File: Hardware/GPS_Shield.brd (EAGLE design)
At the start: 59.7 x 53.3 mm, 52 parts, among them J1 ARDUINO_R3_SHIELD, J2 USD_CONNECTOR, J3 DNP (GP-735-VERTICAL), U1 APK2112-3.3V, U2 GP3906-TLP, U3 TXB0108

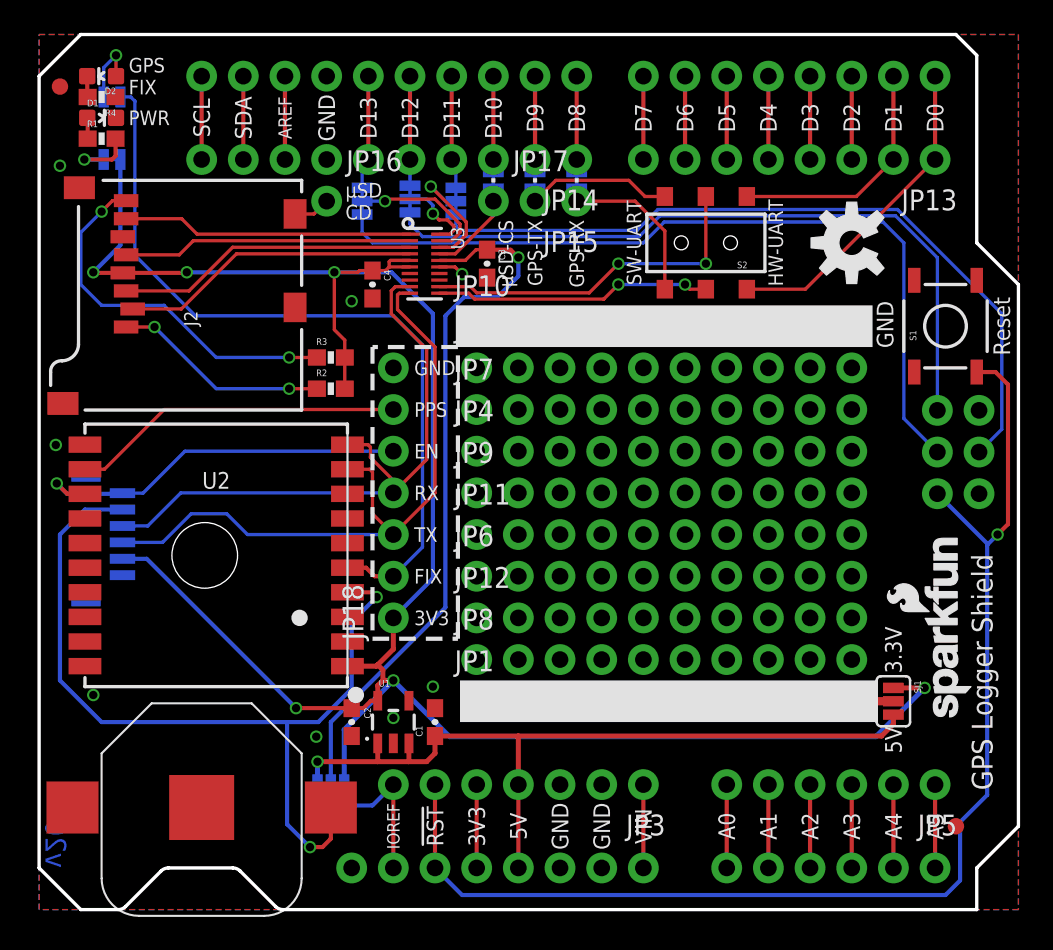
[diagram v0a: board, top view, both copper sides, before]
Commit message: Adding VBATT-to-3.3V jumper, breaking out VBATT.
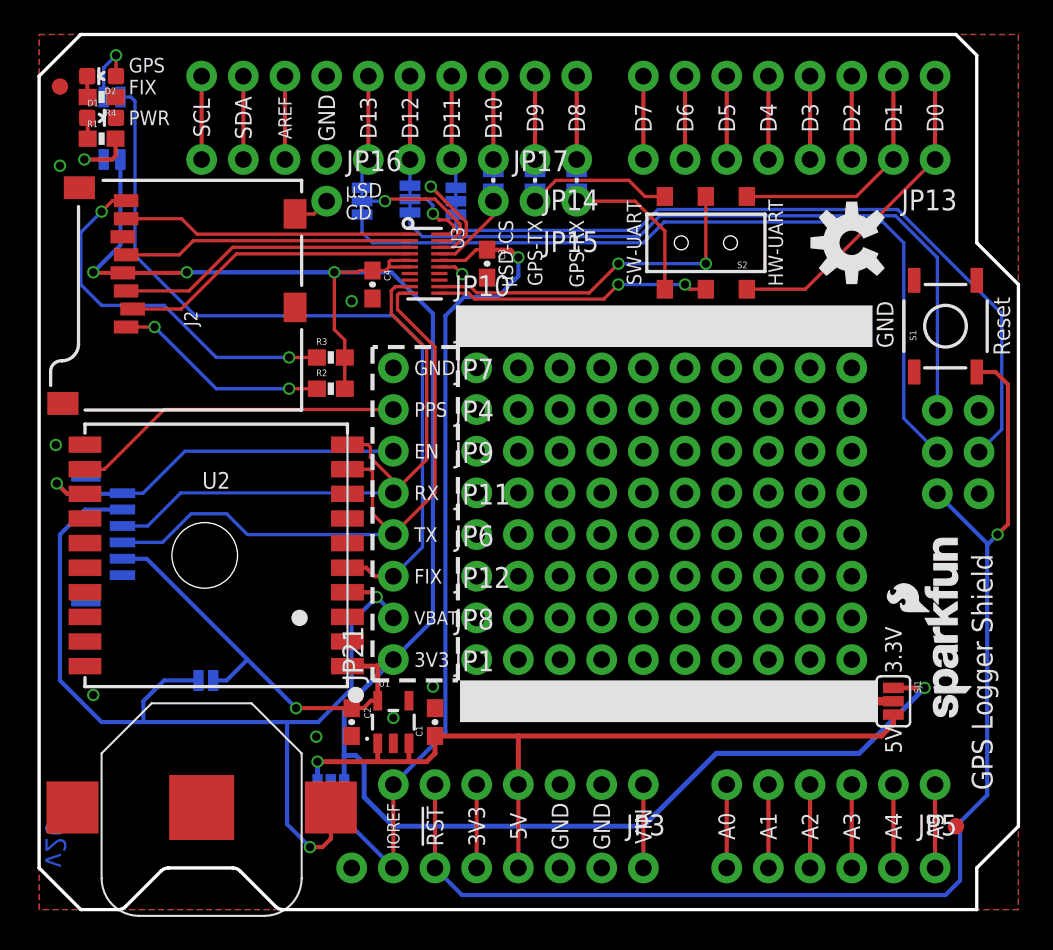
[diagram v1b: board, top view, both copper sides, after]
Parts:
- removed JP18: (no value), SparkFun-Connectors:1X07_NO_SILK
- added JP21: (no value), SparkFun-Connectors:1X08_NO_SILK
- added SJ11: Batt-3v3, SparkFun-Passives:PAD-JUMPER-2-NO_YES_SILK
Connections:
- net 3.3V: now also JP21.1, SJ11.1; no longer JP18.1
- net GND: now also JP21.8; no longer JP18.7
- net GPS_FIX: now also JP21.3; no longer JP18.2
- net GPS_RST: now also JP21.6; no longer JP18.5
- net GPS_RX: now also JP21.5; no longer JP18.4
- net GPS_TX: now also JP21.4; no longer JP18.3
- net PPS: now also JP21.7; no longer JP18.6
- net V_BATT: now also JP21.2, SJ11.2
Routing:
- net 3.3V: track 135.1 -> 145.2 mm, vias 6 -> 5
- net V_BATT: track 52.7 -> 59.6 mm
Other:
- board text added: "Batt"
- board text added: "No Battery"
- board text added: "VBAT"

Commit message: Changing DRU to SparkFun-2-Layer-Tight, slightly moving traces to accomodate.
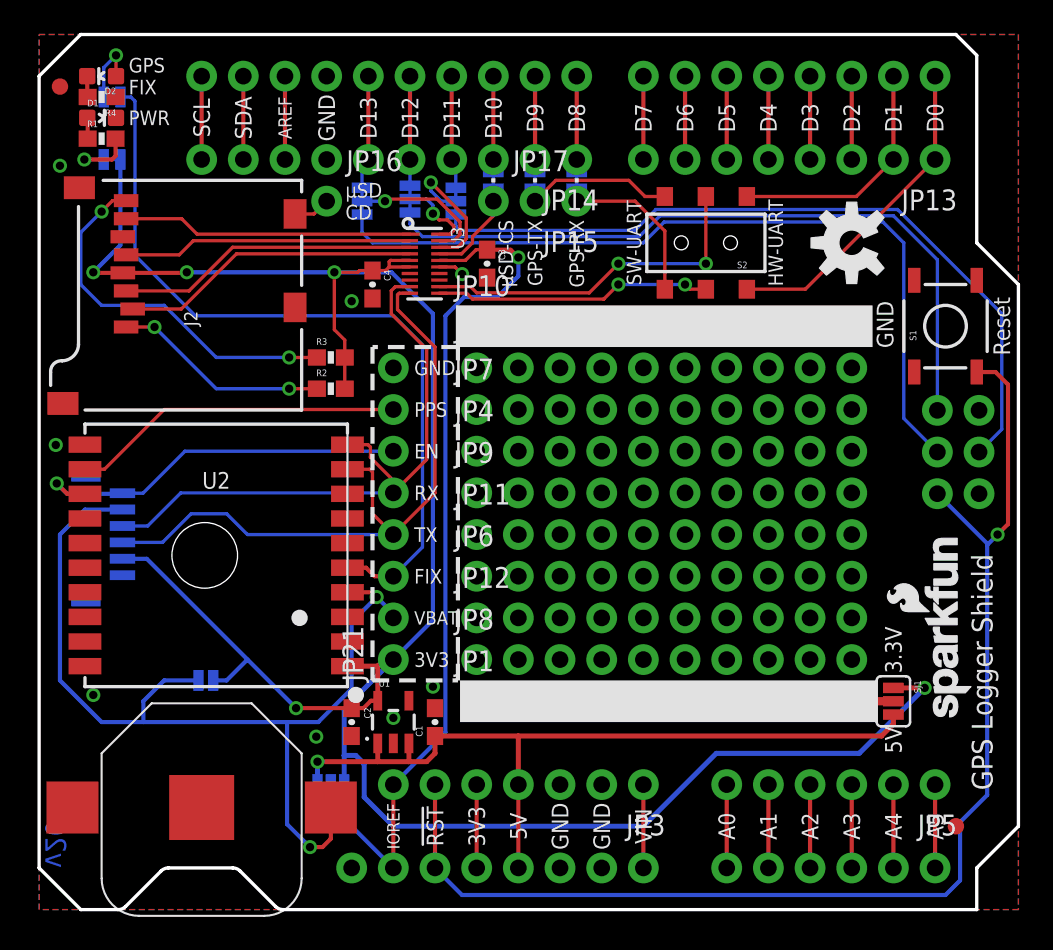
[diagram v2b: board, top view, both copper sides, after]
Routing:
- net HV_MOSI: track 7.67 -> 8.48 mm

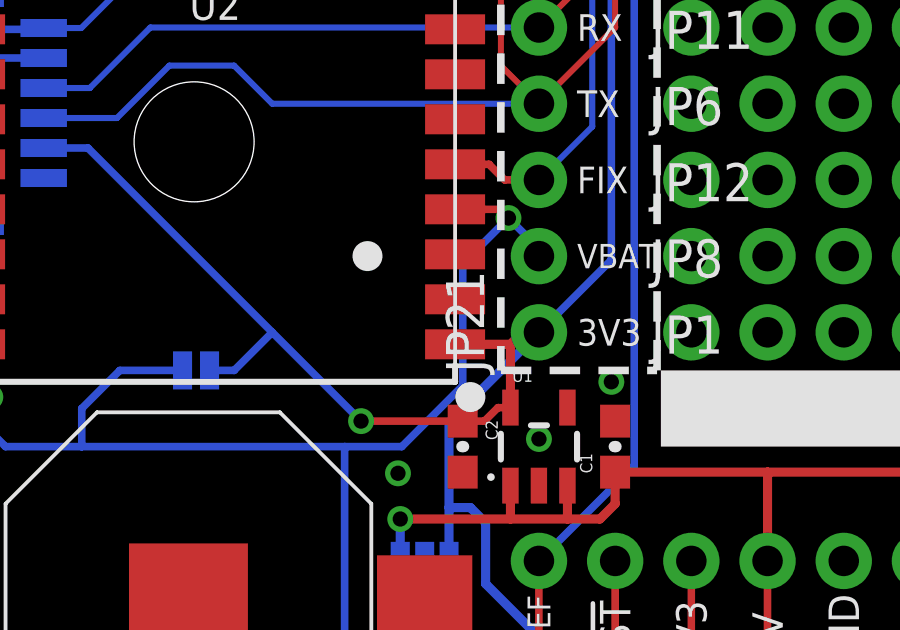
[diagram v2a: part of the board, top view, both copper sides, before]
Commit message: Schematic and trace cleanup.
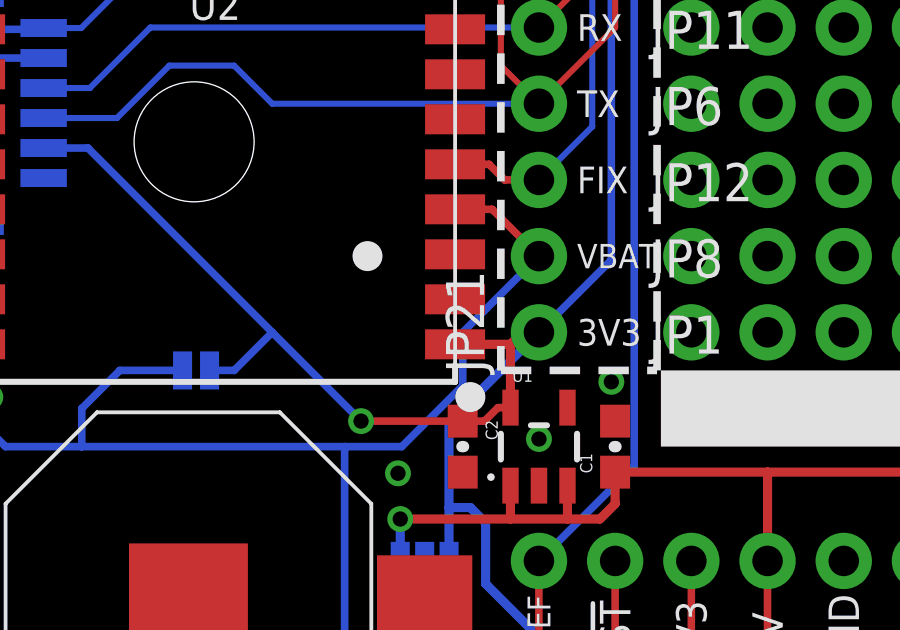
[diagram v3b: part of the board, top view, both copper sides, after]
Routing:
- net V_BATT: track 59.6 -> 58.6 mm, vias 2 -> 1
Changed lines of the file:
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@@
 <via x="15.66" y="12.28" extent="1-16" drill="0.508"/>
 <wire x1="12.7" y1="15.24" x2="15.66" y2="12.28" width="0.254" layer="16"/>
-<wire x1="15.66" y1="12.28" x2="19.05" y2="12.28" width="0.254" layer="1"/>
 <wire x1="19.773" y1="12.28" x2="19.05" y2="12.28" width="0.254" layer="1"/>
 <contactref element="SJ11" pad="1"/>
@@
 <wire x1="19.812" y1="8.89" x2="19.304" y2="9.398" width="0.3048" layer="16"/>
 <wire x1="19.304" y1="9.398" x2="18.5928" y2="9.398" width="0.3048" layer="16"/>
+<wire x1="19.05" y1="12.28" x2="15.66" y2="12.28" width="0.254" layer="1"/>
 </signal>
 <signal name="5V">
@@
 <wire x1="6.35" y1="11.43" x2="15.113" y2="11.43" width="0.254" layer="16"/>
 <wire x1="15.113" y1="11.43" x2="17.018" y2="11.43" width="0.254" layer="16"/>
-<wire x1="18.795" y1="19.34" x2="20.284" y2="19.34" width="0.254" layer="1"/>
-<wire x1="20.284" y1="19.34" x2="20.574" y2="19.05" width="0.254" layer="1"/>
-<via x="20.574" y="19.05" extent="1-16" drill="0.508"/>
-<wire x1="20.574" y1="19.05" x2="19.05" y2="17.526" width="0.254" layer="16"/>
-<wire x1="19.05" y1="17.526" x2="19.05" y2="13.462" width="0.254" layer="16"/>
 <wire x1="19.05" y1="13.462" x2="17.018" y2="11.43" width="0.254" layer="16"/>
 <wire x1="15.113" y1="11.43" x2="15.113" y2="5.207" width="0.254" layer="16"/>
@@
 <wire x1="6.35" y1="12.7" x2="6.35" y2="11.43" width="0.254" layer="16"/>
 <contactref element="JP21" pad="2"/>
-<wire x1="21.59" y1="17.78" x2="21.59" y2="18.034" width="0.254" layer="16"/>
-<wire x1="21.59" y1="18.034" x2="20.574" y2="19.05" width="0.254" layer="16"/>
+<wire x1="18.795" y1="19.34" x2="20.03" y2="19.34" width="0.254" layer="1"/>
+<wire x1="20.03" y1="19.34" x2="21.59" y2="17.78" width="0.254" layer="1"/>
+<wire x1="21.59" y1="17.78" x2="19.05" y2="15.24" width="0.254" layer="16"/>
+<wire x1="19.05" y1="15.24" x2="19.05" y2="13.462" width="0.254" layer="16"/>
 </signal>
 <signal name="CD">

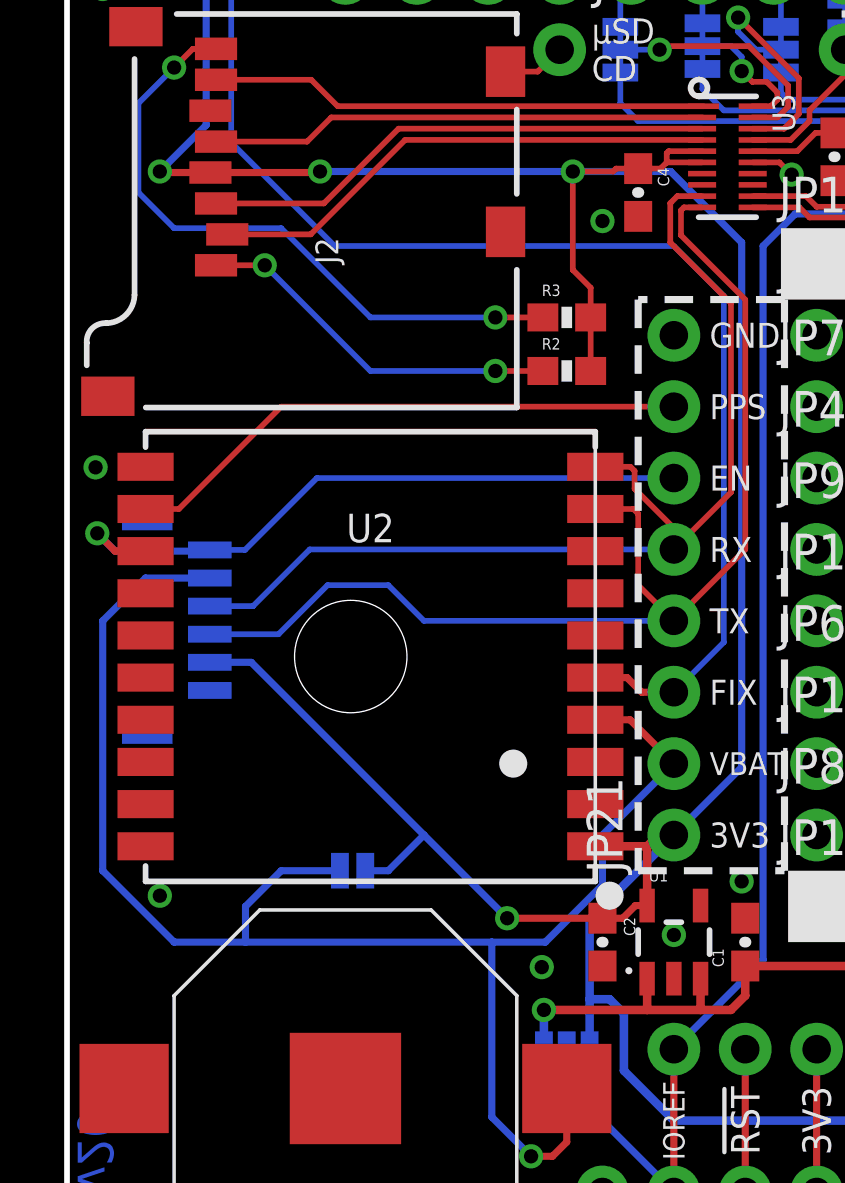
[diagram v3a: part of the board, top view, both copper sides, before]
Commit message: Removing GP-735 fp. Default 3.3/VBat jumper closed.
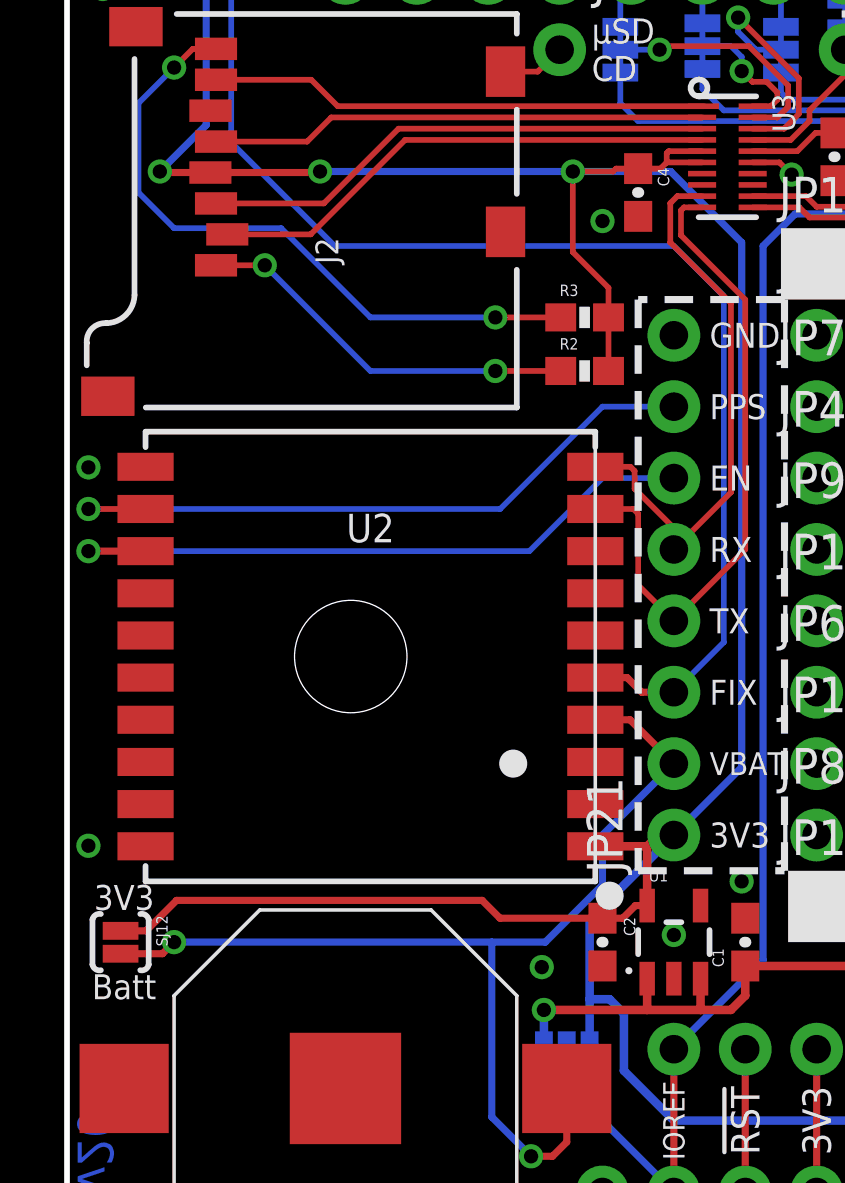
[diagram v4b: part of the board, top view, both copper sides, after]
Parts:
- removed J3: DNP (GP-735-VERTICAL), SparkFun-RF:EM406
- removed SJ11: Batt-3v3, SparkFun-Passives:PAD-JUMPER-2-NO_YES_SILK
- added SJ12: VBAT-3.3V, SparkFun-Passives:PAD-JUMPER-2-NC_BY_PASTE_YES_SILK
- moved R2 0.63 mm to (18.4, 31.8)
- moved R3 0.63 mm to (18.4, 33.7)
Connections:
- net 3.3V: now also SJ12.1; no longer J3.2, SJ11.1
- net GND: no longer J3.1
- net GPS_RST: no longer J3.6
- net GPS_RX: no longer J3.4
- net GPS_TX: no longer J3.3
- net V_BATT: now also SJ12.2; no longer J3.5, SJ11.2
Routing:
- net V_BATT: track 58.6 -> 38.6 mm, vias 1 -> 2
- net GPS_TX: track 41.1 -> 23.3 mm
- net GPS_RX: track 37.5 -> 20.1 mm
- net PPS: track 20.3 -> 24.4 mm, vias 0 -> 1
- net 3.3V: track 145.2 -> 142.9 mm, vias 5 -> 4
- net N$19: track 23.0 -> 23.6 mm
- net N$18: track 13.2 -> 13.8 mm
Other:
- board text removed: "GP-735"
- board text removed: "No Battery"

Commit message: Schematic cleanup
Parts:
- renumbered SJ12 to SJ11
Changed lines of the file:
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@@
 <attribute name="PROD_ID" value="CONN-08438" x="21.59" y="15.24" size="1.778" layer="27" font="vector" ratio="15" rot="R90" display="off"/>
 </element>
-<element name="SJ12" library="SparkFun-Passives" package="PAD-JUMPER-2-NC_BY_PASTE_YES_SILK" value="VBAT-3.3V" x="1.905" y="11.43" rot="R270"/>
+<element name="SJ11" library="SparkFun-Passives" package="PAD-JUMPER-2-NC_BY_PASTE_YES_SILK" value="VBAT-3.3V" x="1.905" y="11.43" rot="R270"/>
 </elements>
 <signals>
@@
 <wire x1="19.304" y1="9.398" x2="18.5928" y2="9.398" width="0.3048" layer="16"/>
 <wire x1="17.995" y1="35.98" x2="19.265" y2="34.71" width="0.2032" layer="1"/>
-<contactref element="SJ12" pad="1"/>
+<contactref element="SJ11" pad="1"/>
 <wire x1="19.05" y1="12.28" x2="15.406" y2="12.28" width="0.254" layer="1"/>
 <wire x1="15.406" y1="12.28" x2="14.771" y2="12.915" width="0.254" layer="1"/>
@@
 <wire x1="21.59" y1="17.78" x2="19.05" y2="15.24" width="0.254" layer="16"/>
 <wire x1="19.05" y1="15.24" x2="19.05" y2="13.462" width="0.254" layer="16"/>
-<contactref element="SJ12" pad="2"/>
+<contactref element="SJ11" pad="2"/>
 <wire x1="1.905" y1="11.0173" x2="3.3973" y2="11.0173" width="0.254" layer="1"/>
 <wire x1="3.3973" y1="11.0173" x2="3.81" y2="11.43" width="0.254" layer="1"/>

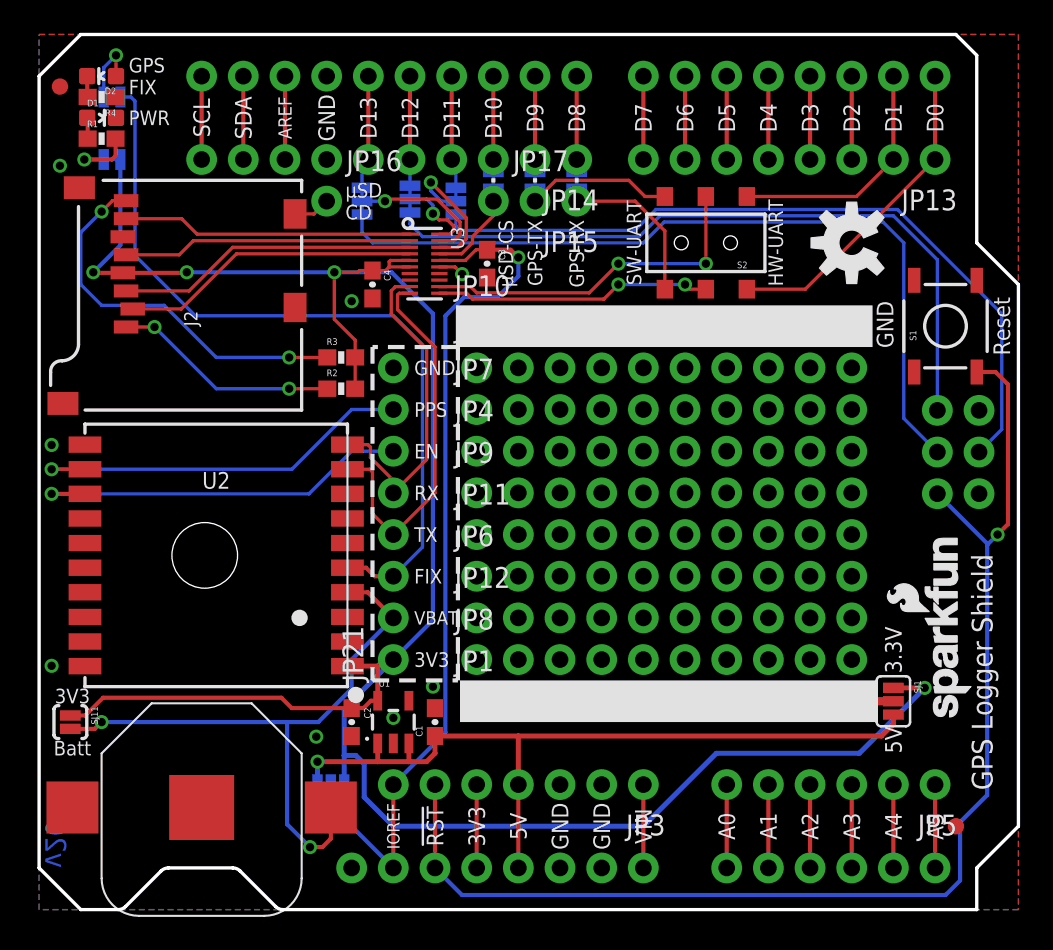
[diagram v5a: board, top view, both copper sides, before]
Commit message: Silkscreen adjustments.
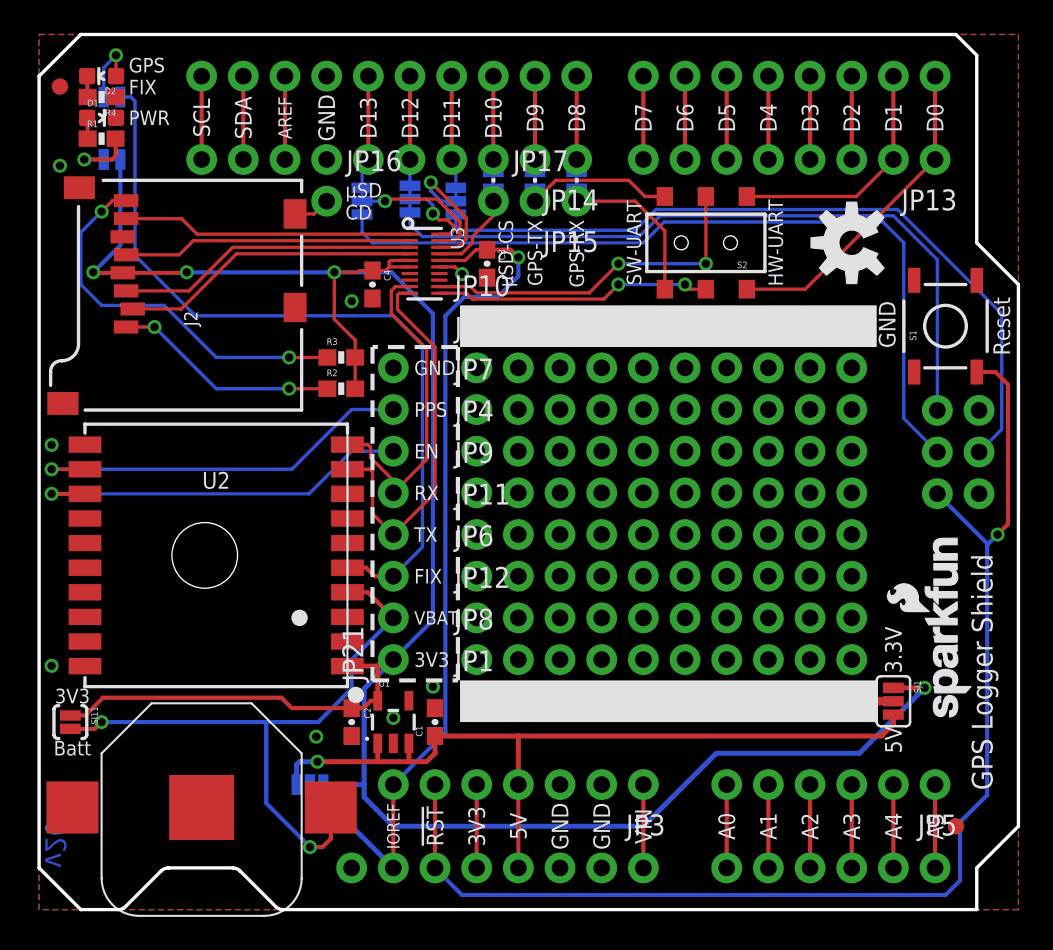
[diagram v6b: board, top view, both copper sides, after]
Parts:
- moved SJ3 1.27 mm to (16.5, 7.62)
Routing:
- net IOREF: track 53.5 -> 54.8 mm
- net 5V: track 48.9 -> 50.1 mm
- net 3.3V: track 142.9 -> 142.2 mm
- net V_BATT: track 38.6 -> 39.1 mm
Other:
- board text added: "5V/3.3V"
